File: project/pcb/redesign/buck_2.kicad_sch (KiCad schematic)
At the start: 15 parts, among them U1 IR2110STRPBF, U2 78M05, U3 SN74HCT14DR

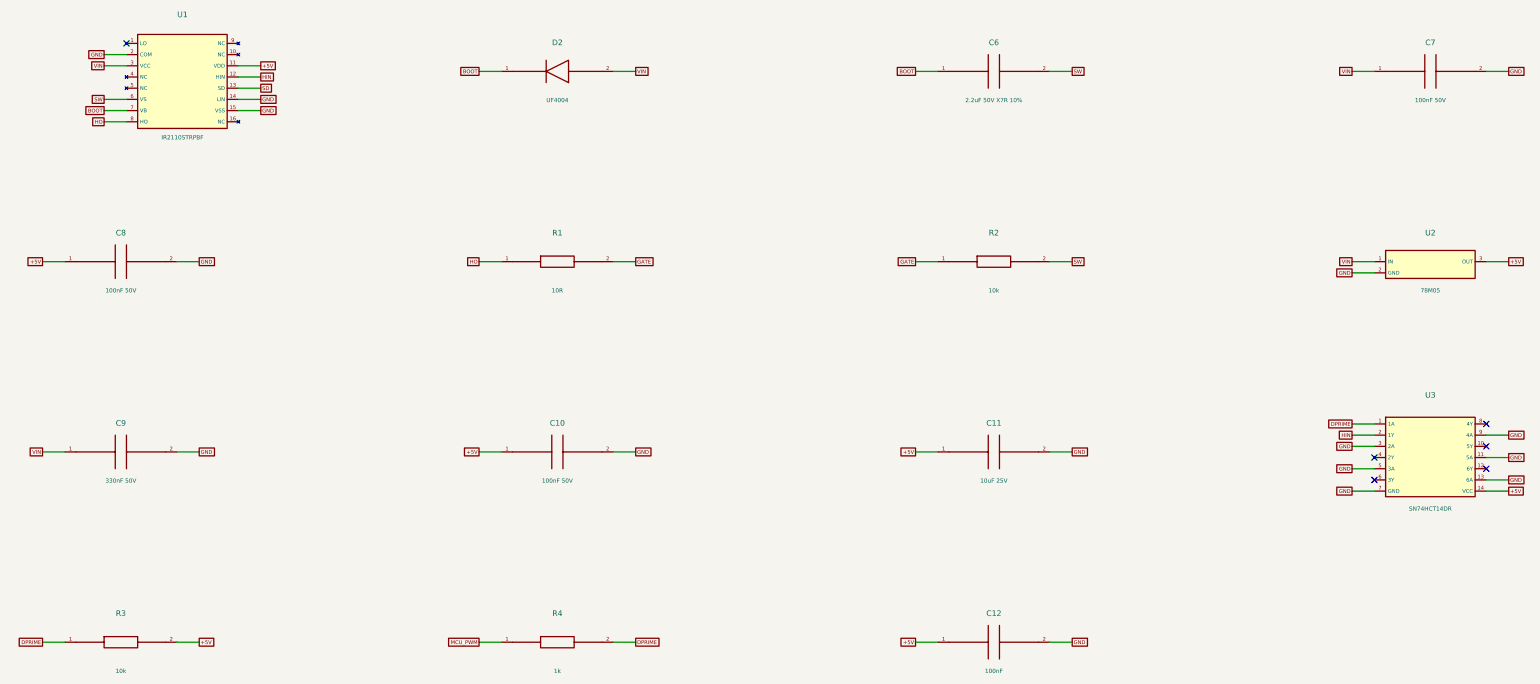
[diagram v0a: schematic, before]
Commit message: feat: Buck PCB Rev B prototype package for JLCPCB
Rev B of project/pcb/redesign, prepared for a JLCPCB top-side SMT quote
and still pending bring-up. Rev A is preserved in history/revA_quote_20261027.

- Lands taken from manufacturer drawings (Murata 6000B, Same Sky TB002,
  Wurth WR-BHD, Panasonic SVPF/SVF, TA-I RLP, TI PW/DBV/DBZ/D/DBV5, Diodes
  SOD323); Q1 hole 1.4 mm per IPC-2222; U5 courtyard added.
- Power-domain interface: SN74LV4T125 buffer for PWM/RUN/RESET from +5V,
  TMUX1511 on the ADC path, TPS3808G33 supervisor, LM4040 2.5 V reference
  with BAT54WS clamps, fault latch set while the interface is disabled.
- Re-laid board: compact switching cell, no vias on HO/GATE/BOOT/SW,
  Kelvin sensing from RS1 inner edges, GND pours on both layers.
- L432KC firmware: Rev B ADC scale (6.4844 mV/count), VOUT-collapse fault,
  host test.
- Fabrication package production/jlcpcb-revB-2026-10-27: DRC 0 errors,
  0 unconnected, 0 parity; ERC 0 errors.

Not ready to order: L1/L2 have no JLC/LCSC stock, the LM4040 X-variant and
R10 supply need decisions, the JLC viewer rotation check and ARM build are
pending. BUCK_BOARD_REVIEWED stays 0. See revB_release_report.md.

Co-Authored-By: Claude Opus 5.5 <noreply@anthropic.com>
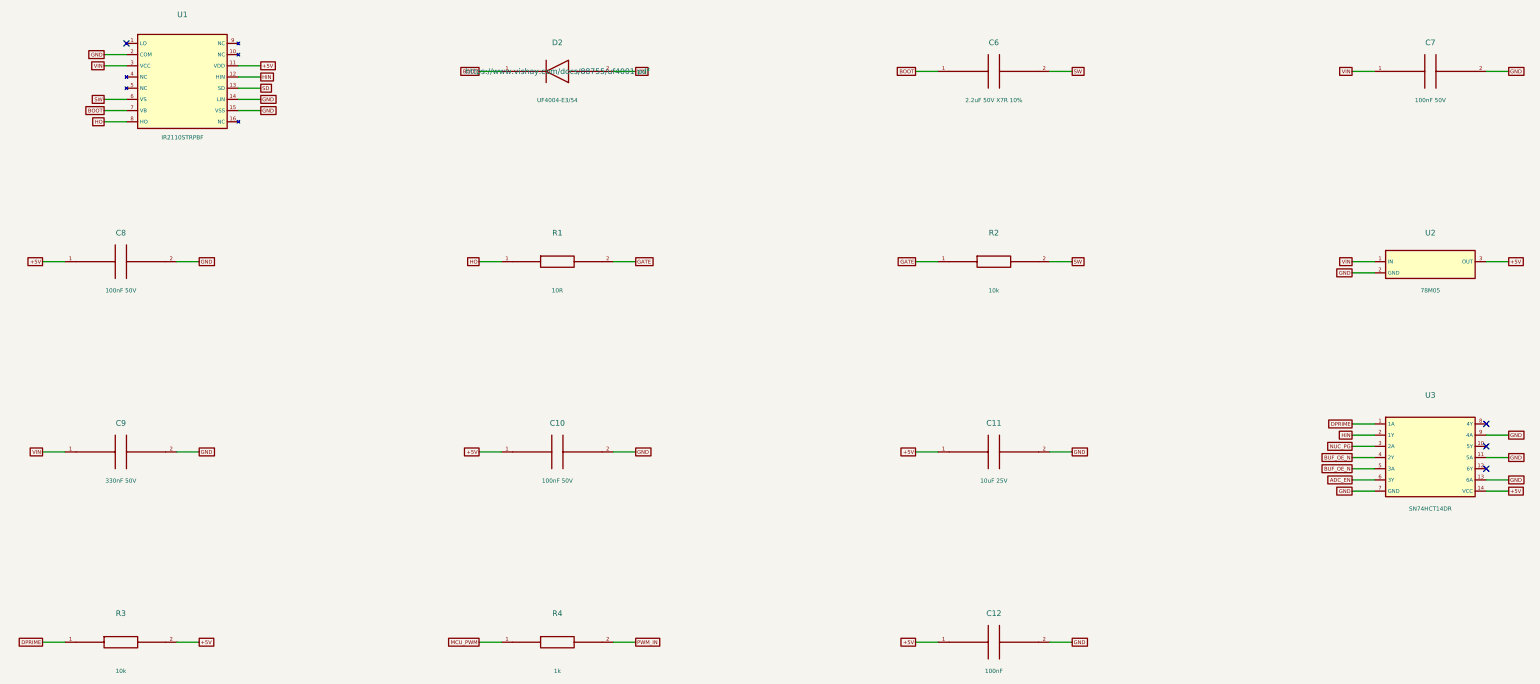
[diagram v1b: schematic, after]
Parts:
- D2: value UF4004 -> UF4004-E3/54; Assembly (none) -> MANUAL_THT; Electrical_Approval PENDING - NOT APPROVED -> PENDING - PROTOTYPE BRING-UP; NOT ELECTRICALLY VALIDATED; LCSC (none) -> C5137033; MPN (none) -> UF4004-E3/54; Manufacturer (none) -> Vishay; Migration_Status BLOCKED / ORIGINAL RETAINED -> REV B - PART FIXED BY RELEASE PLAN
- U3: footprint Buck_SMD:D14 -> Buck_RevB:TI_D0014A_SOIC-14; Migration_Status FOOTPRINT_ONLY / PROVISIONAL - REVIEW REQUIRED -> REV B - LAND CORRECTED TO MANUFACTURER DRAWING
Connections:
- net DPRIME: no longer R4.2
- net GND: no longer U3.3 (2A), U3.5 (3A)
- net BUF_OE_N: now reaches U3.4 (2Y)
- net BUF_OE_N: now also U3.5 (3A)
- net ADC_EN: now reaches U3.6 (3Y)
- new net NUC_PG: U3.3 (2A)
- new net PWM_IN: R4.2
- no-connect marks 6 -> 4
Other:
- title: Gate driver and supplies - REV A / HOLD FABRICATION -> Gate driver and supplies - REV B PROTOTYPE
